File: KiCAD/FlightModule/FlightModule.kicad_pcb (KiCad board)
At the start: 2 copper layers, 90 x 70 mm, 1 part, among them U1 ARDUINO_MKR_WAN_1310

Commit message: 本日の進捗を保存
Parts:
- added U2: MCP2515-xST, Package_SO:TSSOP-20_4.4x6.5mm_P0.65mm, F.Cu at (179.6, 83.4)
- added U3: MCP2562-E-SN, Package_SO:SOIC-8_3.9x4.9mm_P1.27mm, F.Cu at (180.0, 92.5)
- added U4: MB85RQ8MX, Package_SO:SOIC-16W_7.5x10.3mm_P1.27mm, F.Cu at (135.3, 79.4)
- added U5: MB85RQ8MX, Package_SO:SOIC-16W_7.5x10.3mm_P1.27mm, F.Cu at (150.0, 79.4)
- added U6: MB85RQ8MX, Package_SO:SOIC-16W_7.5x10.3mm_P1.27mm, F.Cu at (165.0, 79.3)

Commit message: 大型の部品を配置
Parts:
- added D1: G, LED_SMD:LED_0603_1608Metric_Pad1.05x0.95mm_HandSolder, F.Cu at (45.9, 45.5)
- added D2: GS1010FL, Diode_SMD:D_SOD-123F, F.Cu at (46.4, 39.1)
- added D3: G, LED_SMD:LED_0603_1608Metric_Pad1.05x0.95mm_HandSolder, F.Cu at (65.2, 53.6)
- added D4: GS1010FL, Diode_SMD:D_SOD-123F, F.Cu at (46.4, 42.5)
- added Q1: AO3400A, Package_TO_SOT_SMD:SOT-23, F.Cu at (76.6, 42.9)
- added Q2: AO3400A, Package_TO_SOT_SMD:SOT-23, F.Cu at (76.6, 47.5)
- added R1: 300R, Resistor_SMD:R_0603_1608Metric_Pad0.98x0.95mm_HandSolder, F.Cu at (65.2, 19.9)
- added R2: 10kR, Resistor_SMD:R_0603_1608Metric_Pad0.98x0.95mm_HandSolder, F.Cu at (65.2, 22.4)
- added R3: 2.4kR, Resistor_SMD:R_0603_1608Metric_Pad0.98x0.95mm_HandSolder, F.Cu at (65.2, 24.9)
- added R4: 300R, Resistor_SMD:R_0603_1608Metric_Pad0.98x0.95mm_HandSolder, F.Cu at (65.2, 27.5)
- added R5: 10kR, Resistor_SMD:R_0603_1608Metric_Pad0.98x0.95mm_HandSolder, F.Cu at (65.2, 30.0)
- added R6: 2.4kR, Resistor_SMD:R_0603_1608Metric_Pad0.98x0.95mm_HandSolder, F.Cu at (76.3, 39.2)

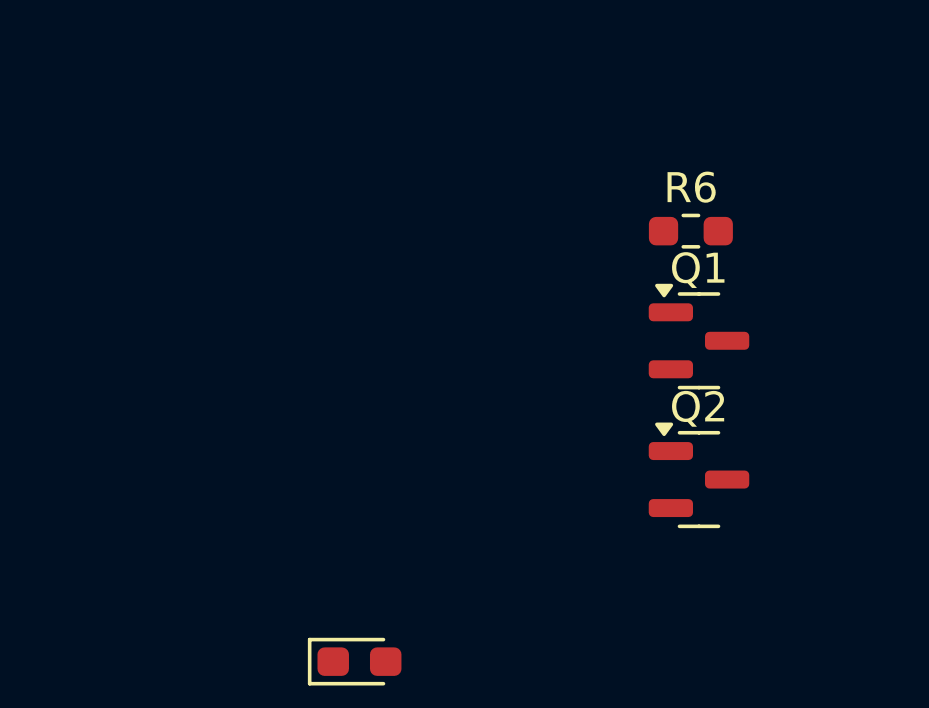
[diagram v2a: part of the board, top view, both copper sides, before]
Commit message: GPSSheildのフットプリントを救出
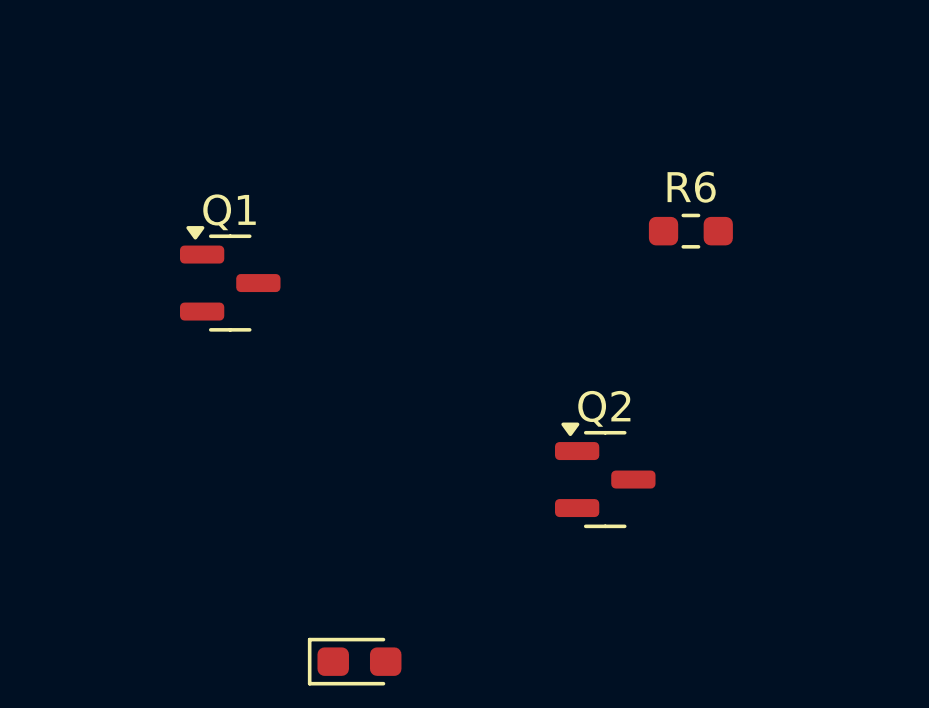
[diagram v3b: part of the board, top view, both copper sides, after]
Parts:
- moved Q1 15.7 mm to (60.9, 41.0)
- moved Q2 3.12 mm to (73.4, 47.5)
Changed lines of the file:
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@@
 	(footprint "Package_TO_SOT_SMD:SOT-23"
 		(layer "F.Cu")
-		(at 76.5625 47.5)
+		(at 73.4375 47.5)
 		(descr "SOT, 3 Pin (JEDEC TO-236 Var AB https://www.jedec.org/document_search?search_api_views_fulltext=TO-236), generated with kicad-footprint-generator ipc_gullwing_generator.py")
 		(tags "SOT TO_SOT_SMD")
@@
 		)
 		(fp_text user "${REFERENCE}"
-			(at 0 0 0)
+			(at -9.0625 0 0)
 			(layer "F.Fab")
 			(effects
@@
 		)
 		(property "Value" "2.4kR"
-			(at 0 1.43 0)
+			(at -15.625 -0.495 0)
 			(layer "F.Fab")
 			(effects
@@
 	(footprint "Package_TO_SOT_SMD:SOT-23"
 		(layer "F.Cu")
-		(at 76.5625 42.875)
+		(at 60.9375 40.95)
 		(descr "SOT, 3 Pin (JEDEC TO-236 Var AB https://www.jedec.org/document_search?search_api_views_fulltext=TO-236), generated with kicad-footprint-generator ipc_gullwing_generator.py")
 		(tags "SOT TO_SOT_SMD")

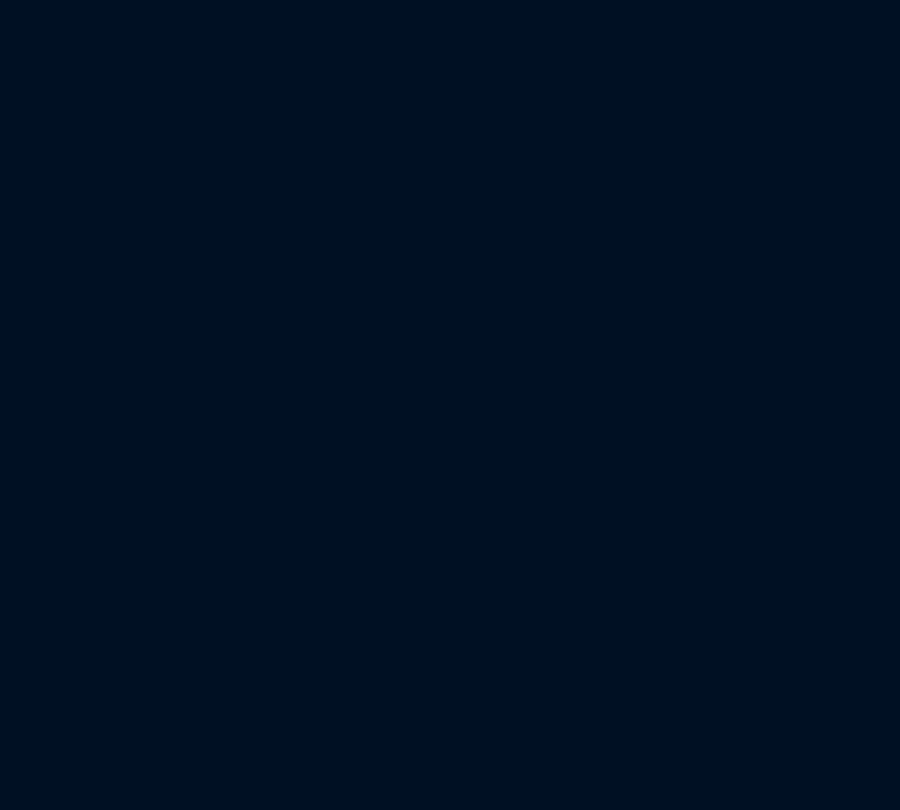
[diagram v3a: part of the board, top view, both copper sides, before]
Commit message: GPSShieldのフットプリントをFlightModuleに移植（手作業☠️）
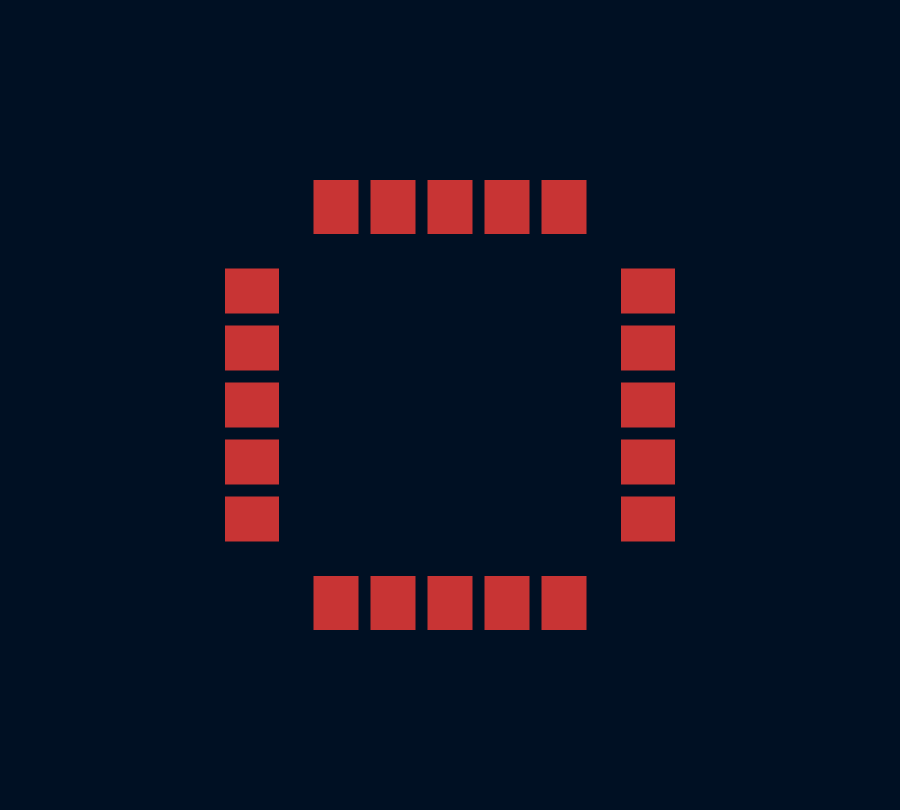
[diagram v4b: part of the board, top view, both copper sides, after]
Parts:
- added IC1: ~, GPSShield:UBLOXLIB_SAM-M8Q, F.Cu at (68.8, 84.5)

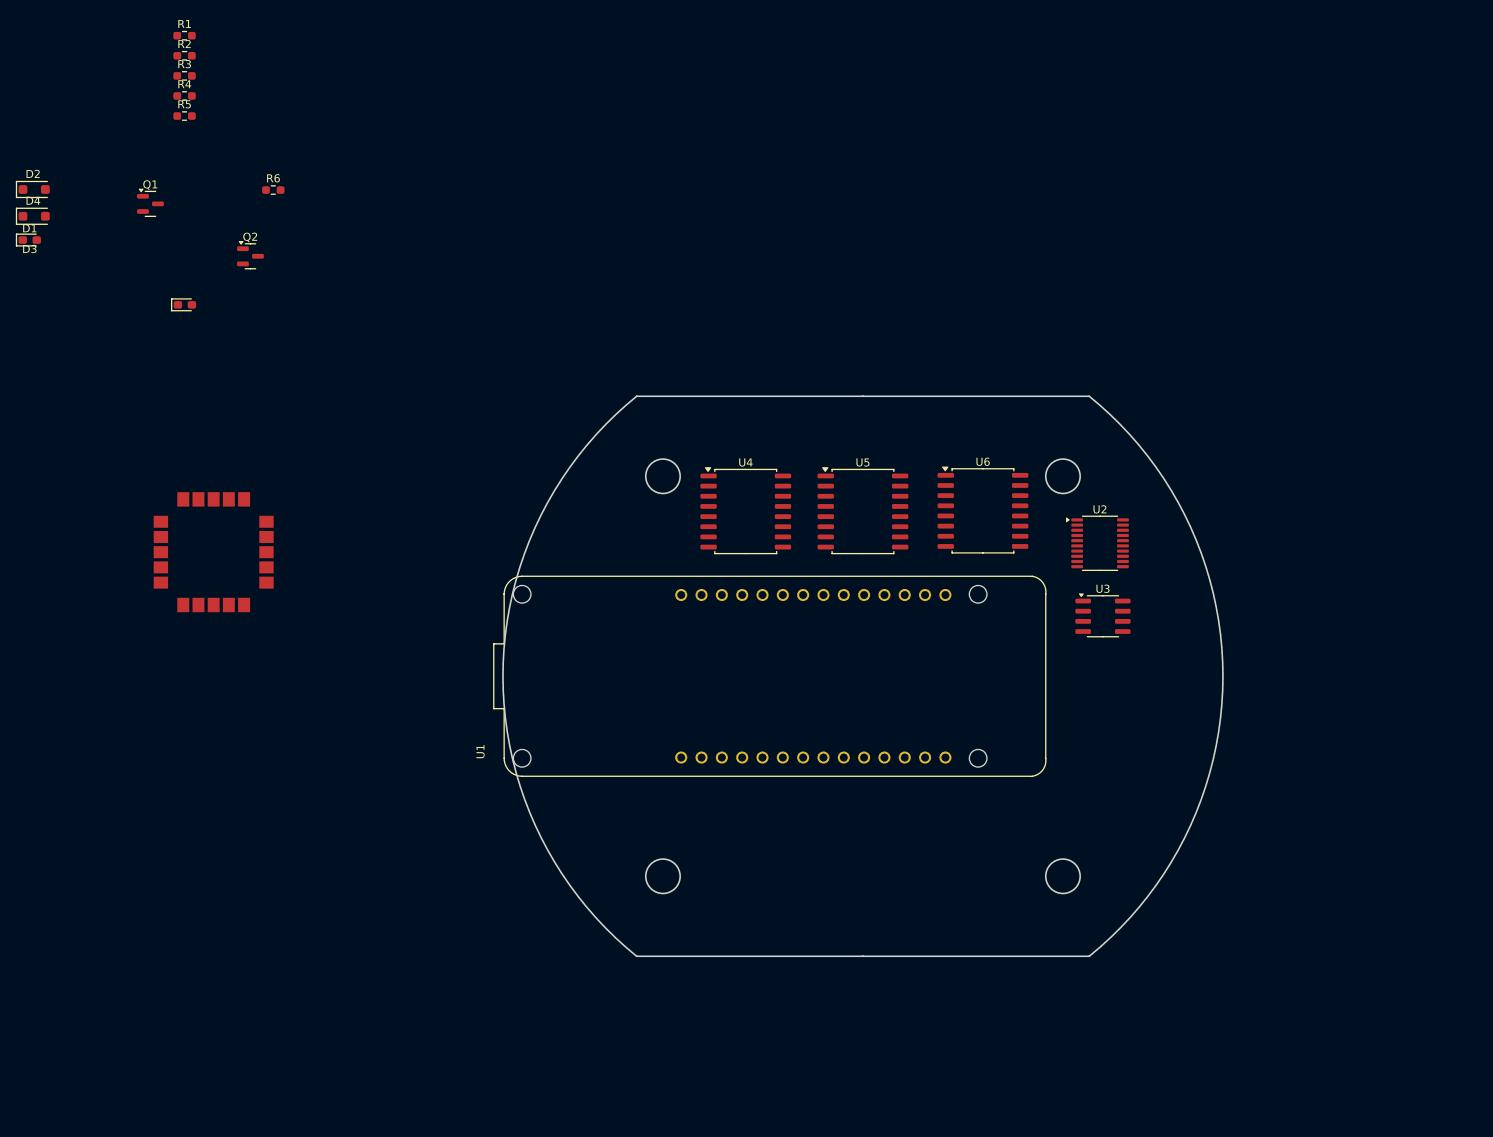
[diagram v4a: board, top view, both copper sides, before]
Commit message: CANトランシーバーの配線完了
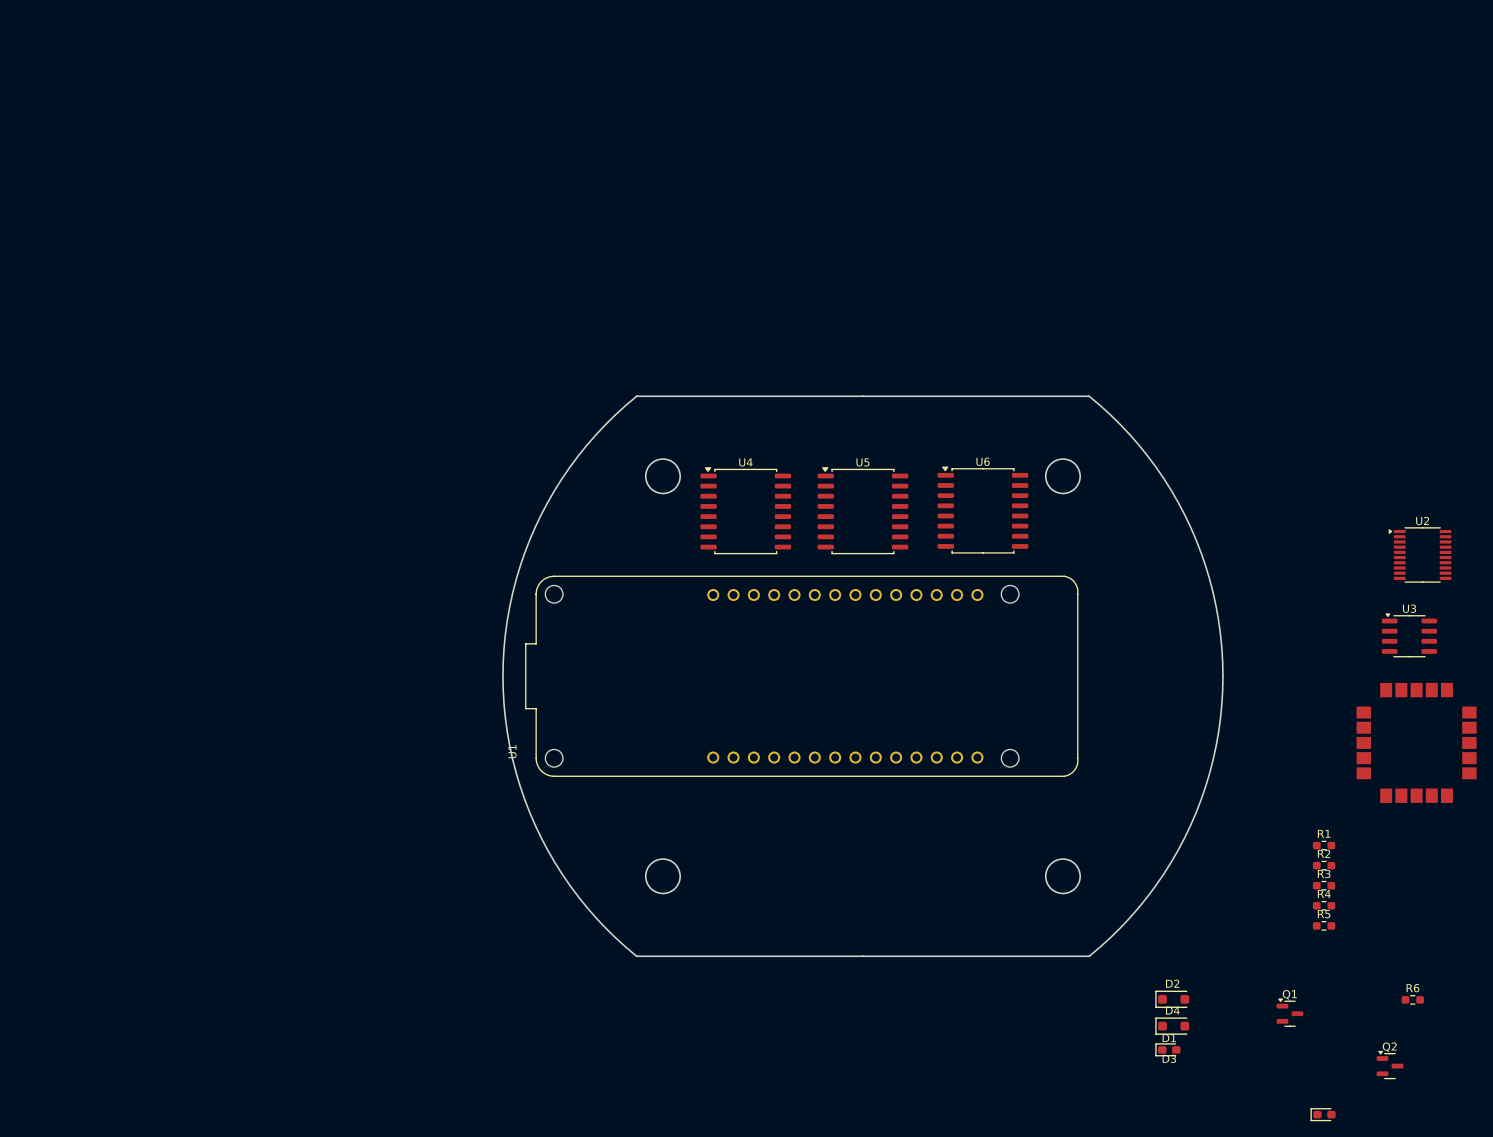
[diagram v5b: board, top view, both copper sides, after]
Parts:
- moved D1 174.7 mm to (188.3, 146.7)
- moved D2 174.7 mm to (188.8, 140.4)
- moved D3 174.7 mm to (207.7, 154.8)
- moved D4 174.7 mm to (188.8, 143.7)
- moved Q1 174.7 mm to (203.4, 142.2)
- moved Q2 174.7 mm to (215.9, 148.7)
- moved R1 174.7 mm to (207.6, 121.2)
- moved R2 174.7 mm to (207.6, 123.7)
- moved R3 174.7 mm to (207.6, 126.2)
- moved R4 174.7 mm to (207.6, 128.7)
- moved R5 174.7 mm to (207.6, 131.2)
- moved R6 174.7 mm to (218.7, 140.4)
- moved IC1 152.2 mm to (219.2, 108.3)
- moved U2 40.4 mm to (220.0, 84.8)
- moved U3 38.4 mm to (218.3, 95.0)
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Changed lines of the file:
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@@
 	(footprint "LED_SMD:LED_0603_1608Metric_Pad1.05x0.95mm_HandSolder"
 		(layer "F.Cu")
-		(at 45.85 45.47)
+		(at 188.288 146.699)
 		(descr "LED SMD 0603 (1608 Metric), square (rectangular) end terminal, IPC_7351 nominal, (Body size source: http://www.tortai-tech.com/upload/download/2011102023233369053.pdf), generated with kicad-footprint-generator")
 		(tags "LED handsolder")
@@
 	(footprint "Resistor_SMD:R_0603_1608Metric_Pad0.98x0.95mm_HandSolder"
 		(layer "F.Cu")
-		(at 65.2 24.95)
+		(at 207.638 126.179)
 		(descr "Resistor SMD 0603 (1608 Metric), square (rectangular) end terminal, IPC_7351 nominal with elongated pad for handsoldering. (Body size source: IPC-SM-782 page 72, https://www.pcb-3d.com/wordpress/wp-content/uploads/ipc-sm-782a_amendment_1_and_2.pdf), generated with kicad-footprint-generator")
 		(tags "resistor handsolder")
@@
 	(footprint "Resistor_SMD:R_0603_1608Metric_Pad0.98x0.95mm_HandSolder"
 		(layer "F.Cu")
-		(at 65.2 27.46)
+		(at 207.638 128.689)
 		(descr "Resistor SMD 0603 (1608 Metric), square (rectangular) end terminal, IPC_7351 nominal with elongated pad for handsoldering. (Body size source: IPC-SM-782 page 72, https://www.pcb-3d.com/wordpress/wp-content/uploads/ipc-sm-782a_amendment_1_and_2.pdf), generated with kicad-footprint-generator")
 		(tags "resistor handsolder")
@@
 	(footprint "LED_SMD:LED_0603_1608Metric_Pad1.05x0.95mm_HandSolder"
 		(layer "F.Cu")
-		(at 65.245 53.57)
+		(at 207.683 154.799)
 		(descr "LED SMD 0603 (1608 Metric), square (rectangular) end terminal, IPC_7351 nominal, (Body size source: http://www.tortai-tech.com/upload/download/2011102023233369053.pdf), generated with kicad-footprint-generator")
 		(tags "LED handsolder")
@@
 	(footprint "Package_TO_SOT_SMD:SOT-23"
 		(layer "F.Cu")
-		(at 73.4375 47.5)
+		(at 215.8755 148.729)
 		(descr "SOT, 3 Pin (JEDEC TO-236 Var AB https://www.jedec.org/document_search?search_api_views_fulltext=TO-236), generated with kicad-footprint-generator ipc_gullwing_generator.py")
 		(tags "SOT TO_SOT_SMD")
@@
 	(footprint "Diode_SMD:D_SOD-123F"
 		(layer "F.Cu")
-		(at 46.4 42.5)
+		(at 188.838 143.729)
 		(descr "D_SOD-123F")
 		(tags "D_SOD-123F")
@@
 	(footprint "Resistor_SMD:R_0603_1608Metric_Pad0.98x0.95mm_HandSolder"
 		(layer "F.Cu")
-		(at 65.2 19.93)
+		(at 207.638 121.159)
 		(descr "Resistor SMD 0603 (1608 Metric), square (rectangular) end terminal, IPC_7351 nominal with elongated pad for handsoldering. (Body size source: IPC-SM-782 page 72, https://www.pcb-3d.com/wordpress/wp-content/uploads/ipc-sm-782a_amendment_1_and_2.pdf), generated with kicad-footprint-generator")
 		(tags "resistor handsolder")
@@
 	(footprint "Diode_SMD:D_SOD-123F"
 		(layer "F.Cu")
-		(at 46.4 39.15)
+		(at 188.838 140.379)
 		(descr "D_SOD-123F")
 		(tags "D_SOD-123F")
@@
 	(footprint "Package_SO:SOIC-8_3.9x4.9mm_P1.27mm"
 		(layer "F.Cu")
-		(at 180 92.5)
+		(at 218.313 94.996)
 		(descr "SOIC, 8 Pin (JEDEC MS-012AA, https://www.analog.com/media/en/package-pcb-resources/package/pkg_pdf/soic_narrow-r/r_8.pdf), generated with kicad-footprint-generator ipc_gullwing_generator.py")
 		(tags "SOIC SO")
@@
 		)
 		(fp_text user "${REFERENCE}"
-			(at 34.84 6.905 0)
+			(at -0.127 5.08 0)
 			(layer "F.Fab")
 			(effects
@@
 		(locked yes)
 		(layer "F.Cu")
-		(at 139 100 90)
+		(at 143 100 90)
 		(property "Reference" "U1"
 			(at -9.425 -36.775 90)
@@
 		)
 		(embedded_fonts no)
+		(model "${KICAD9_3RD_PARTY}/KiCad-Library/TSRP_Arduino/MKR1310.step"
+			(offset
+				(xyz 105 148.5 1.5)
+			)
+			(scale
+				(xyz 1 1 1)
+			)
+			(rotate
+				(xyz -0 -0 90)
+			)
+		)
 	)
 	(footprint "Resistor_SMD:R_0603_1608Metric_Pad0.98x0.95mm_HandSolder"
 		(layer "F.Cu")
-		(at 65.2 29.97)
+		(at 207.638 131.199)
 		(descr "Resistor SMD 0603 (1608 Metric), square (rectangular) end terminal, IPC_7351 nominal with elongated pad for handsoldering. (Body size source: IPC-SM-782 page 72, https://www.pcb-3d.com/wordpress/wp-content/uploads/ipc-sm-782a_amendment_1_and_2.pdf), generated with kicad-footprint-generator")
 		(tags "resistor handsolder")
@@
 	(footprint "Package_SO:TSSOP-20_4.4x6.5mm_P0.65mm"
 		(layer "F.Cu")
-		(at 179.6375 83.375)
+		(at 219.964 84.836)
 		(descr "TSSOP, 20 Pin (JEDEC MO-153 Var AC https://www.jedec.org/document_search?search_api_views_fulltext=MO-153), generated with kicad-footprint-generator ipc_gullwing_generator.py")
 		(tags "TSSOP SO")
@@
 	(footprint "GPSShield:UBLOXLIB_SAM-M8Q"
 		(layer "F.Cu")
-		(at 68.8385 84.4885)
+		(at 219.202 108.331)
 		(property "Reference" "IC1"
 			(at 0 0 0)
@@
 	(footprint "Resistor_SMD:R_0603_1608Metric_Pad0.98x0.95mm_HandSolder"
 		(layer "F.Cu")
-		(at 65.2 22.44)
+		(at 207.638 123.669)
 		(descr "Resistor SMD 0603 (1608 Metric), square (rectangular) end terminal, IPC_7351 nominal with elongated pad for handsoldering. (Body size source: IPC-SM-782 page 72, https://www.pcb-3d.com/wordpress/wp-content/uploads/ipc-sm-782a_amendment_1_and_2.pdf), generated with kicad-footprint-generator")
 		(tags "resistor handsolder")
@@
 	(footprint "Resistor_SMD:R_0603_1608Metric_Pad0.98x0.95mm_HandSolder"
 		(layer "F.Cu")
-		(at 76.2925 39.22)
+		(at 218.7305 140.449)
 		(descr "Resistor SMD 0603 (1608 Metric), square (rectangular) end terminal, IPC_7351 nominal with elongated pad for handsoldering. (Body size source: IPC-SM-782 page 72, https://www.pcb-3d.com/wordpress/wp-content/uploads/ipc-sm-782a_amendment_1_and_2.pdf), generated with kicad-footprint-generator")
 		(tags "resistor handsolder")
@@
 	(footprint "Package_TO_SOT_SMD:SOT-23"
 		(layer "F.Cu")
-		(at 60.9375 40.95)
+		(at 203.3755 142.179)
 		(descr "SOT, 3 Pin (JEDEC TO-236 Var AB https://www.jedec.org/document_search?search_api_views_fulltext=TO-236), generated with kicad-footprint-generator ipc_gullwing_generator.py")
 		(tags "SOT TO_SOT_SMD")
